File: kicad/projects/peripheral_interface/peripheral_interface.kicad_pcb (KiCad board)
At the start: 2 copper layers, 203.2 x 97.8 mm, 23 parts, among them J1 Pi Pico Standin, J2 VOLTAGE CONVERTER, J3 OLED SCREEN, J4 BACKPLANE AUX, J5 BACKPLANE BANK, J6 BACKPLANE BUS, J7 TO CPU, J8 FROM CPU, J9 KEYPAD, U1 74HC595, U10 74HC597, U11 74HCT157, U12 74HCT157, U13 74HCT245, U14 74HC597, U2 74HC595, U3 74HC595, U4 74HC595, U5 74HC595, U6 74HC595, U7 74HC597, U8 74HC597, U9 74HC597

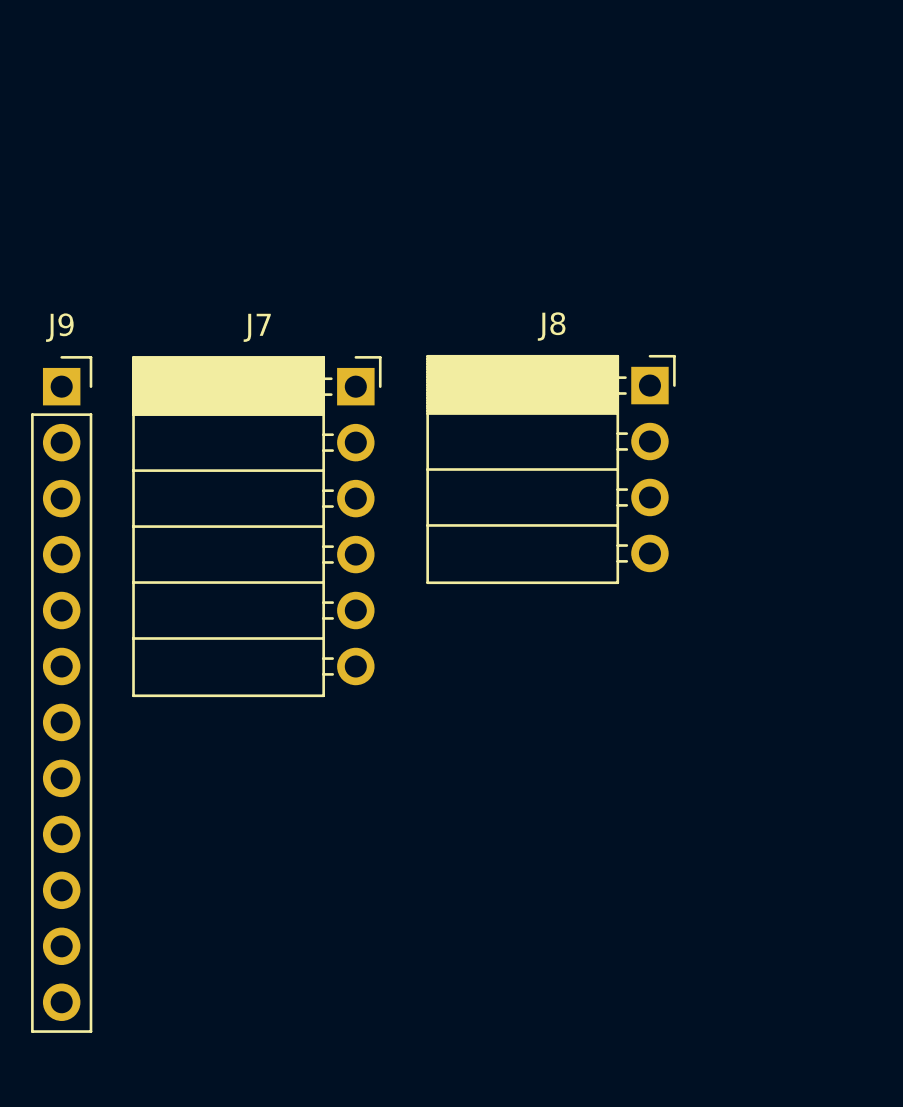
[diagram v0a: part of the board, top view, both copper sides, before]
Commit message: Add latest micropython from running full test in hardware.
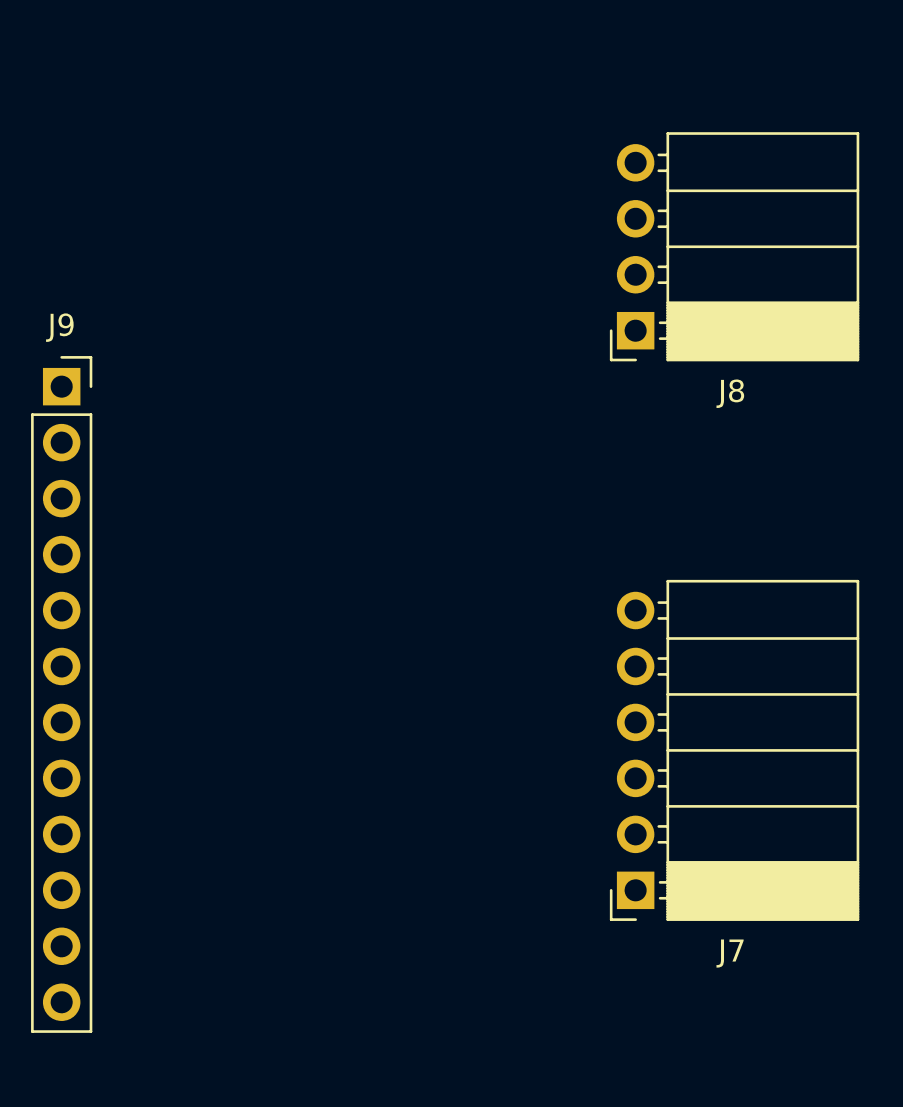
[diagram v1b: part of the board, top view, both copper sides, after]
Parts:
- moved J7 26.2 mm to (292.1, 106.7), turned to 180 degrees
- moved J8 2.57 mm to (292.1, 81.3), turned to 180 degrees
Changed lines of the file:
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@@
   (net 361 "unconnected-(J9-Pad12)")
   (footprint "Connector_PinSocket_2.54mm:PinSocket_1x06_P2.54mm_Horizontal" (layer "F.Cu")
-    (at 279.4 83.82)
+    (at 292.1 106.68 180)
     (descr "Through hole angled socket strip, 1x06, 2.54mm pitch, 8.51mm socket length, single row (from Kicad 4.0.7), script generated")
     (tags "Through hole angled socket strip THT 1x06 2.54mm single row")
@@
     (fp_line (start -1.52 0.3) (end 0 0.3) (layer "F.Fab") (width 0.1))
     (fp_line (start 0 0.3) (end 0 -0.3) (layer "F.Fab") (width 0.1))
-    (pad "1" thru_hole rect (at 0 0) (size 1.7 1.7) (drill 1) (layers *.Cu *.Mask)
+    (pad "1" thru_hole rect (at 0 0 180) (size 1.7 1.7) (drill 1) (layers *.Cu *.Mask)
       (net 340 "unconnected-(J7-Pad1)") (pinfunction "Pin_1") (pintype "passive"))
-    (pad "2" thru_hole oval (at 0 2.54) (size 1.7 1.7) (drill 1) (layers *.Cu *.Mask)
+    (pad "2" thru_hole oval (at 0 2.54 180) (size 1.7 1.7) (drill 1) (layers *.Cu *.Mask)
       (net 341 "unconnected-(J7-Pad2)") (pinfunction "Pin_2") (pintype "passive"))
-    (pad "3" thru_hole oval (at 0 5.08) (size 1.7 1.7) (drill 1) (layers *.Cu *.Mask)
+    (pad "3" thru_hole oval (at 0 5.08 180) (size 1.7 1.7) (drill 1) (layers *.Cu *.Mask)
       (net 342 "unconnected-(J7-Pad3)") (pinfunction "Pin_3") (pintype "passive"))
-    (pad "4" thru_hole oval (at 0 7.62) (size 1.7 1.7) (drill 1) (layers *.Cu *.Mask)
+    (pad "4" thru_hole oval (at 0 7.62 180) (size 1.7 1.7) (drill 1) (layers *.Cu *.Mask)
       (net 343 "unconnected-(J7-Pad4)") (pinfunction "Pin_4") (pintype "passive"))
-    (pad "5" thru_hole oval (at 0 10.16) (size 1.7 1.7) (drill 1) (layers *.Cu *.Mask)
+    (pad "5" thru_hole oval (at 0 10.16 180) (size 1.7 1.7) (drill 1) (layers *.Cu *.Mask)
       (net 344 "unconnected-(J7-Pad5)") (pinfunction "Pin_5") (pintype "passive"))
-    (pad "6" thru_hole oval (at 0 12.7) (size 1.7 1.7) (drill 1) (layers *.Cu *.Mask)
+    (pad "6" thru_hole oval (at 0 12.7 180) (size 1.7 1.7) (drill 1) (layers *.Cu *.Mask)
       (net 345 "unconnected-(J7-Pad6)") (pinfunction "Pin_6") (pintype "passive"))
     (model "${KICAD6_3DMODEL_DIR}/Connector_PinSocket_2.54mm.3dshapes/PinSocket_1x06_P2.54mm_Horizontal.wrl"
@@
   )
   (footprint "Connector_PinSocket_2.54mm:PinSocket_1x04_P2.54mm_Horizontal" (layer "F.Cu")
-    (at 292.75 83.77)
+    (at 292.1 81.28 180)
     (descr "Through hole angled socket strip, 1x04, 2.54mm pitch, 8.51mm socket length, single row (from Kicad 4.0.7), script generated")
     (tags "Through hole angled socket strip THT 1x04 2.54mm single row")
@@
     (fp_line (start 0 -0.3) (end -1.52 -0.3) (layer "F.Fab") (width 0.1))
     (fp_line (start -1.52 2.84) (end 0 2.84) (layer "F.Fab") (width 0.1))
-    (pad "1" thru_hole rect (at 0 0) (size 1.7 1.7) (drill 1) (layers *.Cu *.Mask)
+    (pad "1" thru_hole rect (at 0 0 180) (size 1.7 1.7) (drill 1) (layers *.Cu *.Mask)
       (net 346 "unconnected-(J8-Pad1)") (pinfunction "Pin_1") (pintype "passive"))
-    (pad "2" thru_hole oval (at 0 2.54) (size 1.7 1.7) (drill 1) (layers *.Cu *.Mask)
+    (pad "2" thru_hole oval (at 0 2.54 180) (size 1.7 1.7) (drill 1) (layers *.Cu *.Mask)
       (net 347 "unconnected-(J8-Pad2)") (pinfunction "Pin_2") (pintype "passive"))
-    (pad "3" thru_hole oval (at 0 5.08) (size 1.7 1.7) (drill 1) (layers *.Cu *.Mask)
+    (pad "3" thru_hole oval (at 0 5.08 180) (size 1.7 1.7) (drill 1) (layers *.Cu *.Mask)
       (net 348 "unconnected-(J8-Pad3)") (pinfunction "Pin_3") (pintype "passive"))
-    (pad "4" thru_hole oval (at 0 7.62) (size 1.7 1.7) (drill 1) (layers *.Cu *.Mask)
+    (pad "4" thru_hole oval (at 0 7.62 180) (size 1.7 1.7) (drill 1) (layers *.Cu *.Mask)
       (net 349 "unconnected-(J8-Pad4)") (pinfunction "Pin_4") (pintype "passive"))
     (model "${KICAD6_3DMODEL_DIR}/Connector_PinSocket_2.54mm.3dshapes/PinSocket_1x04_P2.54mm_Horizontal.wrl"

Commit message: Starting on PCB layout for peripheral interface.
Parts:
- added C1: C, Capacitor_THT:C_Disc_D4.7mm_W2.5mm_P5.00mm, F.Cu at (142.2, -50.8)
- added C10: C, Capacitor_THT:C_Disc_D4.7mm_W2.5mm_P5.00mm, F.Cu at (125.9, -50.6)
- added C11: C, Capacitor_THT:C_Disc_D4.7mm_W2.5mm_P5.00mm, F.Cu at (142.2, -42.7)
- added C12: C, Capacitor_THT:C_Disc_D4.7mm_W2.5mm_P5.00mm, F.Cu at (134.1, -42.5)
- added C13: C, Capacitor_THT:C_Disc_D4.7mm_W2.5mm_P5.00mm, F.Cu at (208.3, 83.8)
- added C14: C, Capacitor_THT:C_Disc_D4.7mm_W2.5mm_P5.00mm, F.Cu at (156.2, -54.9)
- added C15: C_Polarized, Capacitor_THT:CP_Radial_D6.3mm_P2.50mm, F.Cu at (151.6, -48.9)
- added C16: C_Polarized, Capacitor_THT:CP_Radial_D6.3mm_P2.50mm, F.Cu at (151.6, -41.0)
- added C17: C_Polarized, Capacitor_THT:CP_Radial_D6.3mm_P2.50mm, F.Cu at (159.6, -48.9)
- added C2: C, Capacitor_THT:C_Disc_D4.7mm_W2.5mm_P5.00mm, F.Cu at (139.8, -54.9)
- added C3: C, Capacitor_THT:C_Disc_D4.7mm_W2.5mm_P5.00mm, F.Cu at (142.2, -46.8)
- added C4: C, Capacitor_THT:C_Disc_D4.7mm_W2.5mm_P5.00mm, F.Cu at (139.7, -22.9)
- added C5: C, Capacitor_THT:C_Disc_D4.7mm_W2.5mm_P5.00mm, F.Cu at (134.1, -50.6)
- added C6: C, Capacitor_THT:C_Disc_D4.7mm_W2.5mm_P5.00mm, F.Cu at (125.9, -46.5)
- added C7: C, Capacitor_THT:C_Disc_D4.7mm_W2.5mm_P5.00mm, F.Cu at (134.1, -46.5)
- added C8: C, Capacitor_THT:C_Disc_D4.7mm_W2.5mm_P5.00mm, F.Cu at (148.0, -54.9)
- added C9: C, Capacitor_THT:C_Disc_D4.7mm_W2.5mm_P5.00mm, F.Cu at (125.9, -42.5)
- added D1: 1N5819, Diode_THT:D_DO-41_SOD81_P10.16mm_Horizontal, F.Cu at (126.2, -54.8)
- moved J9 202.8 mm to (63.5, 73.4), turned to 90 degrees
- moved U6 126.5 mm to (213.4, 63.5)
- moved U5 124.0 mm to (182.9, 63.5)
- moved U3 112.1 mm to (61.0, 86.4)
- moved U13 105.8 mm to (116.8, 63.5), turned to 90 degrees
- moved U14 100.1 mm to (152.4, 63.5), turned to 90 degrees
- moved U2 70.3 mm to (91.4, 114.3)
- moved U11 52.8 mm to (182.9, 86.4)
- moved J8 52.5 mm to (247.3, 108.8)
- moved J7 49.3 mm to (247.8, 85.1)
- moved U12 29.3 mm to (213.4, 86.4)
- moved U9 28.4 mm to (121.9, 86.4)
- moved U7 28.4 mm to (121.9, 114.3)
- moved U4 28.1 mm to (91.4, 86.4)
- moved U10 7.62 mm to (152.4, 86.4)
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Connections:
- J1 pad 1: unconnected-(J1-Pad1) -> /KP_ROW_0
- J1 pad 10: unconnected-(J1-Pad10) -> /KP_COLUMN_3
- J1 pad 11: unconnected-(J1-Pad11) -> /KP_COLUMN_4
- J1 pad 12: unconnected-(J1-Pad12) -> /KP_COLUMN_5
- J1 pad 13: unconnected-(J1-Pad13) -> GND
- J1 pad 14: unconnected-(J1-Pad14) -> /KP_COLUMN_6
- J1 pad 15: unconnected-(J1-Pad15) -> /KP_COLUMN_7
- J1 pad 16: unconnected-(J1-Pad16) -> /SERIAL_READ_STORAGE_CLK_3V3
- J1 pad 17: unconnected-(J1-Pad17) -> /SERIAL_READ_PARALLEL_LOAD_3V3
- J1 pad 18: unconnected-(J1-Pad18) -> GND
- J1 pad 19: unconnected-(J1-Pad19) -> /SERIAL_READ_SHIFT_CLK_3V3
- J1 pad 2: unconnected-(J1-Pad2) -> /KP_ROW_1
- J1 pad 20: unconnected-(J1-Pad20) -> /SERIAL_WRITE_DATA_3V3
- J1 pad 21: unconnected-(J1-Pad21) -> /SERIAL_WRITE_SHIFT_CLK_3V3
- J1 pad 22: unconnected-(J1-Pad22) -> /SERIAL_WRITE_OUT_CLK_3V3
- J1 pad 23: unconnected-(J1-Pad23) -> GND
- J1 pad 24: unconnected-(J1-Pad24) -> /CLK_PULSE_3V3
- J1 pad 26: unconnected-(J1-Pad26) -> /SCREEN_SDA
- J1 pad 27: unconnected-(J1-Pad27) -> /SCREEN_SCL
- J1 pad 28: unconnected-(J1-Pad28) -> GND
- J1 pad 29: unconnected-(J1-Pad29) -> /SERIAL_READ_DATA_3V3
- J1 pad 3: unconnected-(J1-Pad3) -> GND
- J1 pad 33: unconnected-(J1-Pad33) -> GND
- J1 pad 36: unconnected-(J1-Pad36) -> /3V3_FROM_PICO
- J1 pad 38: unconnected-(J1-Pad38) -> GND
- J1 pad 39: unconnected-(J1-Pad39) -> Net-(D1-Pad1)
- J1 pad 4: unconnected-(J1-Pad4) -> /KP_ROW_2
- J1 pad 40: unconnected-(J1-Pad40) -> VCC
- J1 pad 5: unconnected-(J1-Pad5) -> /KP_ROW_3
- J1 pad 6: unconnected-(J1-Pad6) -> /KP_COLUMN_0
- J1 pad 7: unconnected-(J1-Pad7) -> /KP_COLUMN_1
- J1 pad 8: unconnected-(J1-Pad8) -> GND
- J1 pad 9: unconnected-(J1-Pad9) -> /KP_COLUMN_2
- J2 pad 1: unconnected-(J2-Pad1) -> /SERIAL_READ_DATA_3V3
- J2 pad 12: unconnected-(J2-Pad12) -> /SERIAL_READ_DATA_5V
- J2 pad 3: unconnected-(J2-Pad3) -> /3V3_FROM_PICO
- J3 pad 3: VCC -> /3V3_FROM_PICO
- J7 pad 1: unconnected-(J7-Pad1) -> /ADDR_OE_TO_CPU
- J7 pad 2: unconnected-(J7-Pad2) -> /DATA_OE_TO_CPU
- J7 pad 3: unconnected-(J7-Pad3) -> /CLK_EN_TO_CPU
- J7 pad 4: unconnected-(J7-Pad4) -> /CLK_SEL_TO_CPU
- J7 pad 5: unconnected-(J7-Pad5) -> /CLK_PULSE_5V
- J7 pad 6: unconnected-(J7-Pad6) -> /RESET
- J8 pad 1: unconnected-(J8-Pad1) -> /WTM_FROM_CPU
- J8 pad 2: unconnected-(J8-Pad2) -> /RFM_FROM_CPU
- J8 pad 3: unconnected-(J8-Pad3) -> /DATA_CLK_FROM_CPU
- J8 pad 4: unconnected-(J8-Pad4) -> /CTL_CLK_FROM_CPU
- J9 pad 1: unconnected-(J9-Pad1) -> /KP_ROW_0
- J9 pad 10: unconnected-(J9-Pad10) -> /KP_COLUMN_5
- J9 pad 11: unconnected-(J9-Pad11) -> /KP_COLUMN_6
- J9 pad 12: unconnected-(J9-Pad12) -> /KP_COLUMN_7
- J9 pad 2: unconnected-(J9-Pad2) -> /KP_ROW_1
- J9 pad 3: unconnected-(J9-Pad3) -> /KP_ROW_2
- J9 pad 4: unconnected-(J9-Pad4) -> /KP_ROW_3
- J9 pad 5: unconnected-(J9-Pad5) -> /KP_COLUMN_0
- J9 pad 6: unconnected-(J9-Pad6) -> /KP_COLUMN_1
- J9 pad 7: unconnected-(J9-Pad7) -> /KP_COLUMN_2
- J9 pad 8: unconnected-(J9-Pad8) -> /KP_COLUMN_3
- J9 pad 9: unconnected-(J9-Pad9) -> /KP_COLUMN_4
- U1 pad 1: unconnected-(U1-Pad1) -> /ADDR_BUS_14
- U1 pad 10: unconnected-(U1-Pad10) -> VCC
- U1 pad 11: unconnected-(U1-Pad11) -> /SERIAL_WRITE_SHIFT_CLK_5V
- U1 pad 12: unconnected-(U1-Pad12) -> /SERIAL_WRITE_OUT_CLK_5V
- U1 pad 13: unconnected-(U1-Pad13) -> /INTERFACE_ADDR_ASSERT
- U1 pad 14: unconnected-(U1-Pad14) -> /SERIAL_WRITE_DATA_5V
- U1 pad 15: unconnected-(U1-Pad15) -> /ADDR_BUS_15
- U1 pad 16: unconnected-(U1-Pad16) -> VCC
- U1 pad 2: unconnected-(U1-Pad2) -> /ADDR_BUS_13
- U1 pad 3: unconnected-(U1-Pad3) -> /ADDR_BUS_12
- U1 pad 4: unconnected-(U1-Pad4) -> /ADDR_BUS_11
- U1 pad 5: unconnected-(U1-Pad5) -> /ADDR_BUS_10
- U1 pad 6: unconnected-(U1-Pad6) -> /ADDR_BUS_09
- U1 pad 7: unconnected-(U1-Pad7) -> /ADDR_BUS_08
- U1 pad 8: unconnected-(U1-Pad8) -> GND
- U1 pad 9: unconnected-(U1-Pad9) -> Net-(U1-Pad9)
- U10 pad 1: unconnected-(U10-Pad1) -> /DATA_BUS_06
- U10 pad 10: unconnected-(U10-Pad10) -> VCC
- U10 pad 11: unconnected-(U10-Pad11) -> /SERIAL_READ_SHIFT_CLK_5V
- U10 pad 12: unconnected-(U10-Pad12) -> /SERIAL_READ_STORAGE_CLK_5V
- U10 pad 13: unconnected-(U10-Pad13) -> /SERIAL_READ_PARALLEL_LOAD_5V
- U10 pad 14: unconnected-(U10-Pad14) -> Net-(U10-Pad14)
- U10 pad 15: unconnected-(U10-Pad15) -> /DATA_BUS_07
- U10 pad 16: unconnected-(U10-Pad16) -> VCC
- U10 pad 2: unconnected-(U10-Pad2) -> /DATA_BUS_05
- U10 pad 3: unconnected-(U10-Pad3) -> /DATA_BUS_04
- U10 pad 4: unconnected-(U10-Pad4) -> /DATA_BUS_03
- U10 pad 5: unconnected-(U10-Pad5) -> /DATA_BUS_02
- U10 pad 6: unconnected-(U10-Pad6) -> /DATA_BUS_01
- U10 pad 7: unconnected-(U10-Pad7) -> /DATA_BUS_00
- U10 pad 8: unconnected-(U10-Pad8) -> GND
- U10 pad 9: unconnected-(U10-Pad9) -> Net-(U10-Pad9)
- U11 pad 1: unconnected-(U11-Pad1) -> /RFM_AND_WTM_SEL
- U11 pad 10: unconnected-(U11-Pad10) -> GND
- U11 pad 11: unconnected-(U11-Pad11) -> GND
- U11 pad 13: unconnected-(U11-Pad13) -> GND
- U11 pad 14: unconnected-(U11-Pad14) -> GND
- U11 pad 15: unconnected-(U11-Pad15) -> GND
- U11 pad 16: unconnected-(U11-Pad16) -> VCC
- U11 pad 2: unconnected-(U11-Pad2) -> /RFM_FROM_IFCE
- U11 pad 3: unconnected-(U11-Pad3) -> /RFM_FROM_CPU
- U11 pad 4: unconnected-(U11-Pad4) -> /RFM
- U11 pad 5: unconnected-(U11-Pad5) -> /WTM_FROM_IFCE
- U11 pad 6: unconnected-(U11-Pad6) -> /WTM_FROM_CPU
- U11 pad 7: unconnected-(U11-Pad7) -> /WTM
- U11 pad 8: unconnected-(U11-Pad8) -> GND
- U12 pad 1: unconnected-(U12-Pad1) -> /DATA_AND_CTL_CLK_SEL
- U12 pad 10: unconnected-(U12-Pad10) -> GND
- U12 pad 11: unconnected-(U12-Pad11) -> GND
- U12 pad 13: unconnected-(U12-Pad13) -> GND
- U12 pad 14: unconnected-(U12-Pad14) -> GND
- U12 pad 15: unconnected-(U12-Pad15) -> GND
- U12 pad 16: unconnected-(U12-Pad16) -> VCC
- U12 pad 2: unconnected-(U12-Pad2) -> /CTL_CLK_FROM_IFCE
- U12 pad 3: unconnected-(U12-Pad3) -> /CTL_CLK_FROM_CPU
- U12 pad 4: unconnected-(U12-Pad4) -> /CONTROL_CLK
- U12 pad 5: unconnected-(U12-Pad5) -> /DATA_CLK_FROM_IFCE
- U12 pad 6: unconnected-(U12-Pad6) -> /DATA_CLK_FROM_CPU
- U12 pad 7: unconnected-(U12-Pad7) -> /DATA_CLK
- U12 pad 8: unconnected-(U12-Pad8) -> GND
- U13 pad 1: unconnected-(U13-Pad1) -> VCC
- U13 pad 10: unconnected-(U13-Pad10) -> GND
- U13 pad 12: unconnected-(U13-Pad12) -> /CLK_PULSE_5V
- U13 pad 13: unconnected-(U13-Pad13) -> /SERIAL_WRITE_OUT_CLK_5V
- U13 pad 14: unconnected-(U13-Pad14) -> /SERIAL_WRITE_SHIFT_CLK_5V
- U13 pad 15: unconnected-(U13-Pad15) -> /SERIAL_WRITE_DATA_5V
- U13 pad 16: unconnected-(U13-Pad16) -> /SERIAL_READ_SHIFT_CLK_5V
- U13 pad 17: unconnected-(U13-Pad17) -> /SERIAL_READ_PARALLEL_LOAD_5V
- U13 pad 18: unconnected-(U13-Pad18) -> /SERIAL_READ_STORAGE_CLK_5V
- U13 pad 19: unconnected-(U13-Pad19) -> GND
- U13 pad 2: unconnected-(U13-Pad2) -> /SERIAL_READ_STORAGE_CLK_3V3
- U13 pad 20: unconnected-(U13-Pad20) -> VCC
- U13 pad 3: unconnected-(U13-Pad3) -> /SERIAL_READ_PARALLEL_LOAD_3V3
- U13 pad 4: unconnected-(U13-Pad4) -> /SERIAL_READ_SHIFT_CLK_3V3
- U13 pad 5: unconnected-(U13-Pad5) -> /SERIAL_WRITE_DATA_3V3
- U13 pad 6: unconnected-(U13-Pad6) -> /SERIAL_WRITE_SHIFT_CLK_3V3
- U13 pad 7: unconnected-(U13-Pad7) -> /SERIAL_WRITE_OUT_CLK_3V3
- U13 pad 8: unconnected-(U13-Pad8) -> /CLK_PULSE_3V3
- U13 pad 9: unconnected-(U13-Pad9) -> GND
- U14 pad 1: unconnected-(U14-Pad1) -> /DATA_CLK_FROM_CPU
- U14 pad 10: unconnected-(U14-Pad10) -> VCC
- U14 pad 11: unconnected-(U14-Pad11) -> /SERIAL_READ_SHIFT_CLK_5V
- U14 pad 12: unconnected-(U14-Pad12) -> /SERIAL_READ_STORAGE_CLK_5V
- U14 pad 13: unconnected-(U14-Pad13) -> /SERIAL_READ_PARALLEL_LOAD_5V
- U14 pad 14: unconnected-(U14-Pad14) -> Net-(U10-Pad9)
- U14 pad 15: unconnected-(U14-Pad15) -> /CTL_CLK_FROM_CPU
- U14 pad 16: unconnected-(U14-Pad16) -> VCC
- U14 pad 2: unconnected-(U14-Pad2) -> /RFM_FROM_CPU
- U14 pad 3: unconnected-(U14-Pad3) -> /WTM_FROM_CPU
- U14 pad 4: unconnected-(U14-Pad4) -> GND
- U14 pad 5: unconnected-(U14-Pad5) -> GND
- U14 pad 6: unconnected-(U14-Pad6) -> GND
- U14 pad 7: unconnected-(U14-Pad7) -> GND
- U14 pad 8: unconnected-(U14-Pad8) -> GND
- U14 pad 9: unconnected-(U14-Pad9) -> /SERIAL_READ_DATA_5V
- U2 pad 1: unconnected-(U2-Pad1) -> /ADDR_BUS_06
- U2 pad 10: unconnected-(U2-Pad10) -> VCC
- U2 pad 11: unconnected-(U2-Pad11) -> /SERIAL_WRITE_SHIFT_CLK_5V
- U2 pad 12: unconnected-(U2-Pad12) -> /SERIAL_WRITE_OUT_CLK_5V
- U2 pad 13: unconnected-(U2-Pad13) -> /INTERFACE_ADDR_ASSERT
- U2 pad 14: unconnected-(U2-Pad14) -> Net-(U1-Pad9)
- U2 pad 15: unconnected-(U2-Pad15) -> /ADDR_BUS_07
- U2 pad 16: unconnected-(U2-Pad16) -> VCC
- U2 pad 2: unconnected-(U2-Pad2) -> /ADDR_BUS_05
- U2 pad 3: unconnected-(U2-Pad3) -> /ADDR_BUS_04
- U2 pad 4: unconnected-(U2-Pad4) -> /ADDR_BUS_03
- U2 pad 5: unconnected-(U2-Pad5) -> /ADDR_BUS_02
- U2 pad 6: unconnected-(U2-Pad6) -> /ADDR_BUS_01
- U2 pad 7: unconnected-(U2-Pad7) -> /ADDR_BUS_00
- U2 pad 8: unconnected-(U2-Pad8) -> GND
- U2 pad 9: unconnected-(U2-Pad9) -> Net-(U2-Pad9)
- U3 pad 1: unconnected-(U3-Pad1) -> /DATA_BUS_14
- U3 pad 10: unconnected-(U3-Pad10) -> VCC
- U3 pad 11: unconnected-(U3-Pad11) -> /SERIAL_WRITE_SHIFT_CLK_5V
- U3 pad 12: unconnected-(U3-Pad12) -> /SERIAL_WRITE_OUT_CLK_5V
- U3 pad 13: unconnected-(U3-Pad13) -> /INTERFACE_DATA_ASSERT
- U3 pad 14: unconnected-(U3-Pad14) -> Net-(U2-Pad9)
- U3 pad 15: unconnected-(U3-Pad15) -> /DATA_BUS_15
- U3 pad 16: unconnected-(U3-Pad16) -> VCC
- U3 pad 2: unconnected-(U3-Pad2) -> /DATA_BUS_13
- U3 pad 3: unconnected-(U3-Pad3) -> /DATA_BUS_12
- U3 pad 4: unconnected-(U3-Pad4) -> /DATA_BUS_11
- U3 pad 5: unconnected-(U3-Pad5) -> /DATA_BUS_10
- U3 pad 6: unconnected-(U3-Pad6) -> /DATA_BUS_09
- U3 pad 7: unconnected-(U3-Pad7) -> /DATA_BUS_08
- U3 pad 8: unconnected-(U3-Pad8) -> GND
- U3 pad 9: unconnected-(U3-Pad9) -> Net-(U3-Pad9)
- U4 pad 1: unconnected-(U4-Pad1) -> /DATA_BUS_06
- U4 pad 10: unconnected-(U4-Pad10) -> VCC
- U4 pad 11: unconnected-(U4-Pad11) -> /SERIAL_WRITE_SHIFT_CLK_5V
- U4 pad 12: unconnected-(U4-Pad12) -> /SERIAL_WRITE_OUT_CLK_5V
- U4 pad 13: unconnected-(U4-Pad13) -> /INTERFACE_DATA_ASSERT
- U4 pad 14: unconnected-(U4-Pad14) -> Net-(U3-Pad9)
- U4 pad 15: unconnected-(U4-Pad15) -> /DATA_BUS_07
- U4 pad 16: unconnected-(U4-Pad16) -> VCC
- U4 pad 2: unconnected-(U4-Pad2) -> /DATA_BUS_05
- U4 pad 3: unconnected-(U4-Pad3) -> /DATA_BUS_04
- U4 pad 4: unconnected-(U4-Pad4) -> /DATA_BUS_03
- U4 pad 5: unconnected-(U4-Pad5) -> /DATA_BUS_02
- U4 pad 6: unconnected-(U4-Pad6) -> /DATA_BUS_01
- U4 pad 7: unconnected-(U4-Pad7) -> /DATA_BUS_00
- U4 pad 8: unconnected-(U4-Pad8) -> GND
- U4 pad 9: unconnected-(U4-Pad9) -> Net-(U4-Pad9)
- U5 pad 1: unconnected-(U5-Pad1) -> /DATA_CLK_FROM_IFCE
- U5 pad 10: unconnected-(U5-Pad10) -> VCC
- U5 pad 11: unconnected-(U5-Pad11) -> /SERIAL_WRITE_SHIFT_CLK_5V
- U5 pad 12: unconnected-(U5-Pad12) -> /SERIAL_WRITE_OUT_CLK_5V
- U5 pad 13: unconnected-(U5-Pad13) -> GND
- U5 pad 14: unconnected-(U5-Pad14) -> Net-(U4-Pad9)
- U5 pad 15: unconnected-(U5-Pad15) -> /CTL_CLK_FROM_IFCE
- U5 pad 16: unconnected-(U5-Pad16) -> VCC
- U5 pad 2: unconnected-(U5-Pad2) -> /RFM_FROM_IFCE
- U5 pad 3: unconnected-(U5-Pad3) -> /WTM_FROM_IFCE
- U5 pad 4: unconnected-(U5-Pad4) -> /DATA_AND_CTL_CLK_SEL
- U5 pad 5: unconnected-(U5-Pad5) -> /RFM_AND_WTM_SEL
- U5 pad 6: unconnected-(U5-Pad6) -> /INTERFACE_ADDR_ASSERT
- U5 pad 7: unconnected-(U5-Pad7) -> /INTERFACE_DATA_ASSERT
- U5 pad 8: unconnected-(U5-Pad8) -> GND
- U5 pad 9: unconnected-(U5-Pad9) -> Net-(U5-Pad9)
- U6 pad 1: unconnected-(U6-Pad1) -> /CLK_EN_TO_CPU
- U6 pad 10: unconnected-(U6-Pad10) -> VCC
- U6 pad 11: unconnected-(U6-Pad11) -> /SERIAL_WRITE_SHIFT_CLK_5V
- U6 pad 12: unconnected-(U6-Pad12) -> /SERIAL_WRITE_OUT_CLK_5V
- U6 pad 13: unconnected-(U6-Pad13) -> GND
- U6 pad 14: unconnected-(U6-Pad14) -> Net-(U5-Pad9)
- U6 pad 15: unconnected-(U6-Pad15) -> /RESET
- U6 pad 16: unconnected-(U6-Pad16) -> VCC
- U6 pad 2: unconnected-(U6-Pad2) -> /CLK_SEL_TO_CPU
- U6 pad 3: unconnected-(U6-Pad3) -> /ADDR_OE_TO_CPU
- U6 pad 4: unconnected-(U6-Pad4) -> /DATA_OE_TO_CPU
- U6 pad 8: unconnected-(U6-Pad8) -> GND
- U7 pad 1: unconnected-(U7-Pad1) -> /ADDR_BUS_14
- U7 pad 10: unconnected-(U7-Pad10) -> VCC
- U7 pad 11: unconnected-(U7-Pad11) -> /SERIAL_READ_SHIFT_CLK_5V
- U7 pad 12: unconnected-(U7-Pad12) -> /SERIAL_READ_STORAGE_CLK_5V
- U7 pad 13: unconnected-(U7-Pad13) -> /SERIAL_READ_PARALLEL_LOAD_5V
- U7 pad 14: unconnected-(U7-Pad14) -> GND
- U7 pad 15: unconnected-(U7-Pad15) -> /ADDR_BUS_15
- U7 pad 16: unconnected-(U7-Pad16) -> VCC
- U7 pad 2: unconnected-(U7-Pad2) -> /ADDR_BUS_13
- U7 pad 3: unconnected-(U7-Pad3) -> /ADDR_BUS_12
- U7 pad 4: unconnected-(U7-Pad4) -> /ADDR_BUS_11
- U7 pad 5: unconnected-(U7-Pad5) -> /ADDR_BUS_10
- U7 pad 6: unconnected-(U7-Pad6) -> /ADDR_BUS_09
- U7 pad 7: unconnected-(U7-Pad7) -> /ADDR_BUS_08
- U7 pad 8: unconnected-(U7-Pad8) -> GND
- U7 pad 9: unconnected-(U7-Pad9) -> Net-(U7-Pad9)
- U8 pad 1: unconnected-(U8-Pad1) -> /ADDR_BUS_06
- U8 pad 10: unconnected-(U8-Pad10) -> VCC
- U8 pad 11: unconnected-(U8-Pad11) -> /SERIAL_READ_SHIFT_CLK_5V
- U8 pad 12: unconnected-(U8-Pad12) -> /SERIAL_READ_STORAGE_CLK_5V
- U8 pad 13: unconnected-(U8-Pad13) -> /SERIAL_READ_PARALLEL_LOAD_5V
- U8 pad 14: unconnected-(U8-Pad14) -> Net-(U7-Pad9)
- U8 pad 15: unconnected-(U8-Pad15) -> /ADDR_BUS_07
- U8 pad 16: unconnected-(U8-Pad16) -> VCC
- U8 pad 2: unconnected-(U8-Pad2) -> /ADDR_BUS_05
- U8 pad 3: unconnected-(U8-Pad3) -> /ADDR_BUS_04
- U8 pad 4: unconnected-(U8-Pad4) -> /ADDR_BUS_03
- U8 pad 5: unconnected-(U8-Pad5) -> /ADDR_BUS_02
- U8 pad 6: unconnected-(U8-Pad6) -> /ADDR_BUS_01
- U8 pad 7: unconnected-(U8-Pad7) -> /ADDR_BUS_00
- U8 pad 8: unconnected-(U8-Pad8) -> GND
- U8 pad 9: unconnected-(U8-Pad9) -> Net-(U8-Pad9)
- U9 pad 1: unconnected-(U9-Pad1) -> /DATA_BUS_14
- U9 pad 10: unconnected-(U9-Pad10) -> VCC
- U9 pad 11: unconnected-(U9-Pad11) -> /SERIAL_READ_SHIFT_CLK_5V
- U9 pad 12: unconnected-(U9-Pad12) -> /SERIAL_READ_STORAGE_CLK_5V
- U9 pad 13: unconnected-(U9-Pad13) -> /SERIAL_READ_PARALLEL_LOAD_5V
- U9 pad 14: unconnected-(U9-Pad14) -> Net-(U8-Pad9)
- U9 pad 15: unconnected-(U9-Pad15) -> /DATA_BUS_15
- U9 pad 16: unconnected-(U9-Pad16) -> VCC
- U9 pad 2: unconnected-(U9-Pad2) -> /DATA_BUS_13
- U9 pad 3: unconnected-(U9-Pad3) -> /DATA_BUS_12
- U9 pad 4: unconnected-(U9-Pad4) -> /DATA_BUS_11
- U9 pad 5: unconnected-(U9-Pad5) -> /DATA_BUS_10
- U9 pad 6: unconnected-(U9-Pad6) -> /DATA_BUS_09
- U9 pad 7: unconnected-(U9-Pad7) -> /DATA_BUS_08
- U9 pad 8: unconnected-(U9-Pad8) -> GND
- U9 pad 9: unconnected-(U9-Pad9) -> Net-(U10-Pad14)
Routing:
- net /ADDR_BUS_00: track 0.00 -> 16.0 mm
- net /ADDR_BUS_15: track 0.00 -> 15.7 mm
- net /ADDR_BUS_01: track 0.00 -> 14.3 mm
- net /ADDR_BUS_14: track 0.00 -> 14.2 mm
- net /ADDR_BUS_02: track 0.00 -> 12.9 mm
- net /ADDR_BUS_13: track 0.00 -> 12.5 mm
- net /ADDR_BUS_03: track 0.00 -> 11.4 mm
- net /ADDR_BUS_12: track 0.00 -> 10.9 mm
- net /ADDR_BUS_04: track 0.00 -> 9.90 mm
- net /ADDR_BUS_11: track 0.00 -> 9.29 mm
- net /ADDR_BUS_05: track 0.00 -> 8.42 mm
- net /ADDR_BUS_10: track 0.00 -> 7.66 mm
- net /ADDR_BUS_06: track 0.00 -> 6.94 mm
- net /ADDR_BUS_09: track 0.00 -> 6.03 mm
- net /ADDR_BUS_07: track 0.00 -> 5.61 mm
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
